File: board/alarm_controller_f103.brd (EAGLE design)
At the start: 90 x 65 mm, 147 parts, among them IC3 AT24C, U1 STM32F10XRXT6, X1 RJ45-8L21-S, X2 RJ45-8L21-S

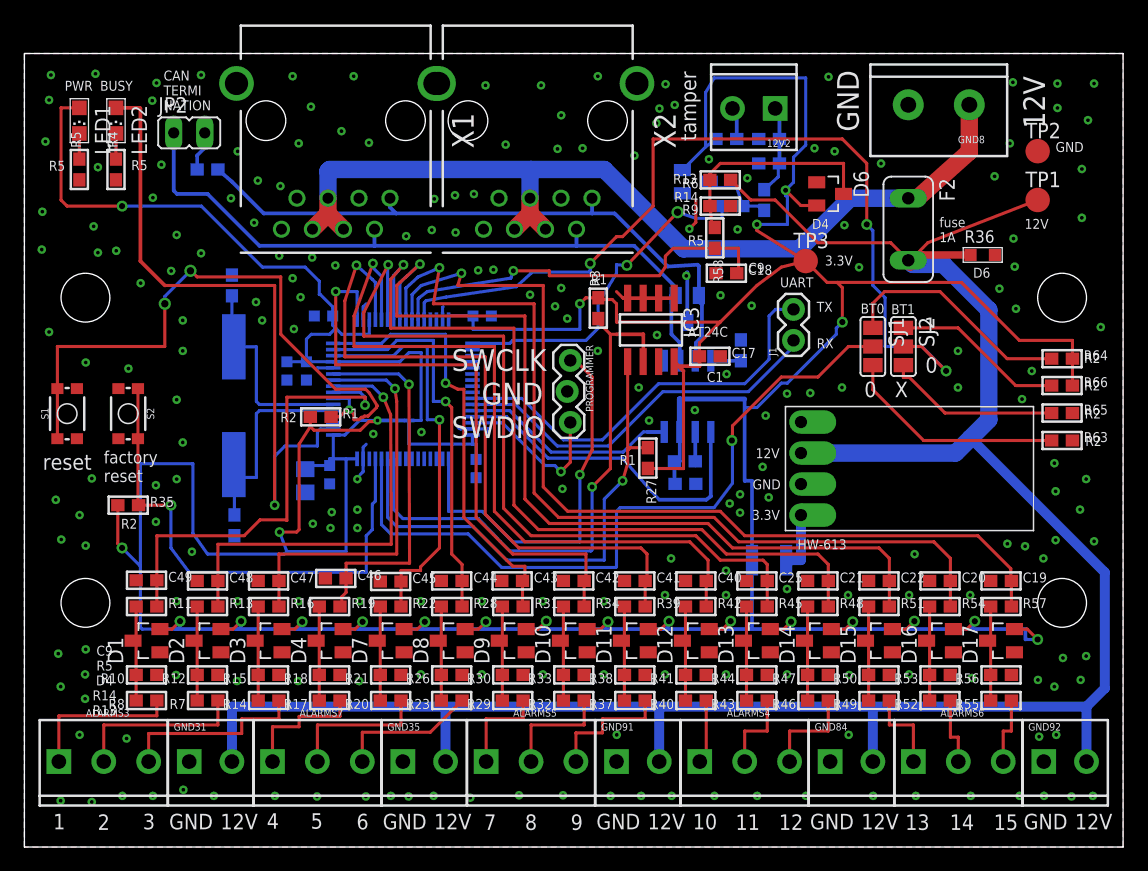
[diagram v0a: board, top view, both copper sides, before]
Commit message: add 3.3v to swd connector
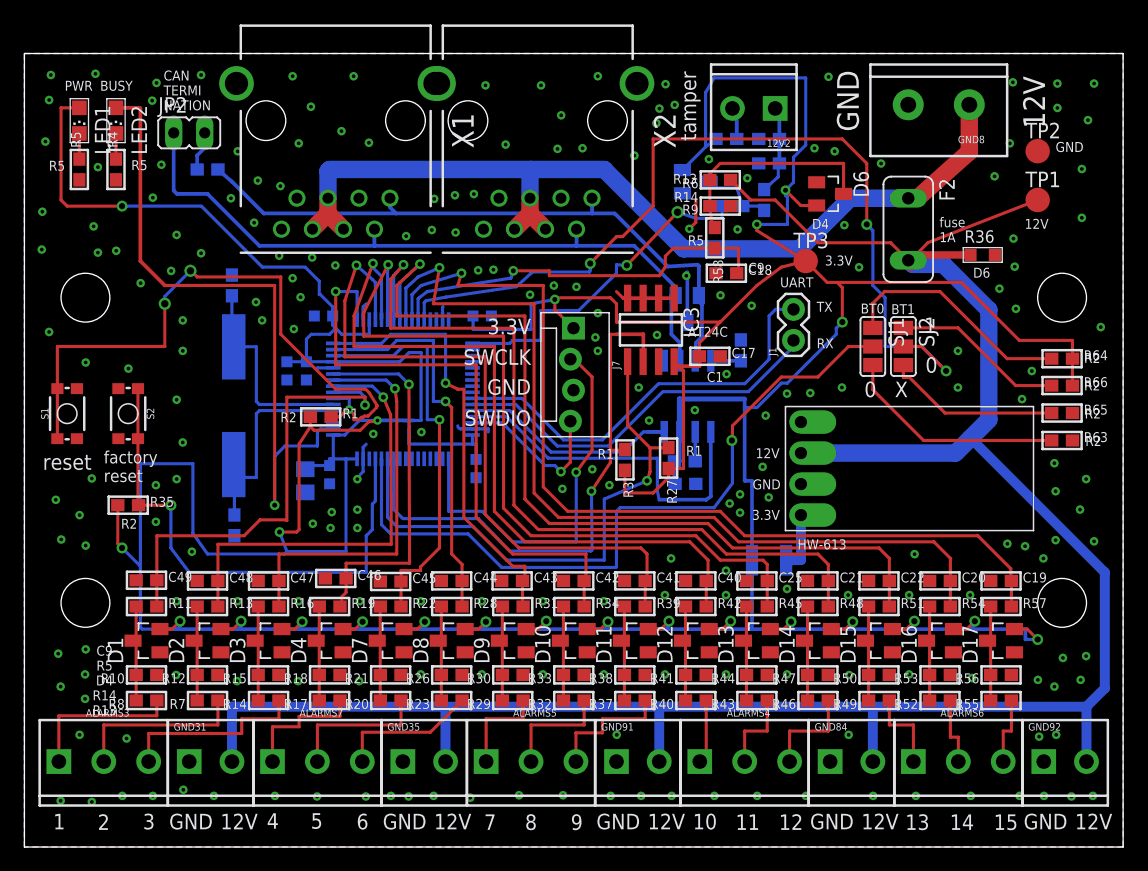
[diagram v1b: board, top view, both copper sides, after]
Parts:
- removed PROGRAMMER: (no value), SparkFun-Connectors:1X03_LOCK
- added J7: (no value), SparkFun-Connectors:MOLEX-1X4_LOCK
- moved R3 12.6 mm to (49.2, 31.7), turned to 270 degrees
- moved R27 1.70 mm to (52.8, 31.9)
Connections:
- net +3V3: now also J7.1
- net GND: now also J7.3; no longer PROGRAMMER.2
- net SWCLK: now also J7.2; no longer PROGRAMMER.1
- net SWDIO: now also J7.4; no longer PROGRAMMER.3
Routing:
- net +3V3: track 446.4 -> 454.3 mm
- net I2C1_SDA: track 42.7 -> 44.9 mm
- net CAN_TX: track 27.8 -> 29.6 mm
- net I2C1_SCL: track 46.8 -> 46.2 mm
- net GND: vias 217 -> 220
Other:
- board text added: "alarm controller 2021.11.13 v1.9"
- board text removed: "alarm controller 2021.06.16 v1.8"
